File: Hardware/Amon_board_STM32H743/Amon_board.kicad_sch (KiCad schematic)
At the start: 4 parts

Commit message: Update: finished routing of PCB_v3
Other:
- sheet Devices ports: added CLK_S, CS_OF, MISO_S, MOSI_S, MOT, RST, SCL_S, SDA_S; removed CLK, MISO, MOSI, SCL, SDA
- sheet Microcontroller ports: added AN_BAT_EDF, AN_BAT_MAIN, AN_BUCK_5V, AUX_port, BRD_Led, BUCK_EN_5V, BUCK_EN_7V2, CE1, CE2, CLK_S, CSN1, CSN2, CS_EXT, CS_OF, CS_SD, DRDY, IRQ1, IRQ2, LED_Red, LED_White, MISO_RF, MISO_S, MOSI_RF, MOSI_S, MOT, PWM_EDF, PWM_Servo_X+, PWM_Servo_X-, PWM_Servo_Y+, PWM_Servo_Y-, RGB_Led_B, RGB_Led_G, RGB_Led_R, RST, RX_GPS, SCK_RF, SCL_EXT, SCL_S, SDA_EXT, SDA_S, TX_GPS; removed none
- sheet Outputs ports: added AUX_port, CLK_S, MISO_S, MOSI_S; removed CLK_EXT, MISO_EXT, MOSI_EXT, SCL, SDA
- sheet Power ports: added AN_BAT_MAIN; removed AN_BAT_BRD
- note added: "AMON Board v3"
- moved on the sheet: H1, H2, H3, H4

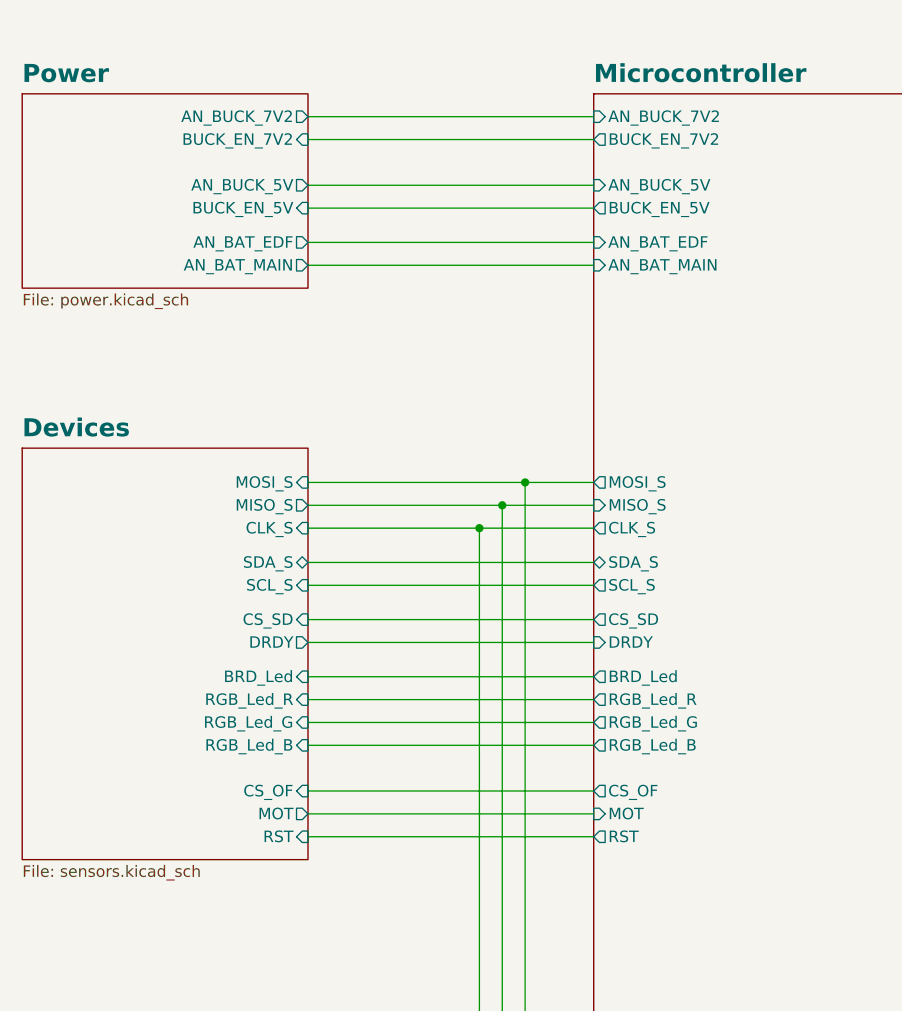
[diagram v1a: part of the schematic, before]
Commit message: Update: finished PCB v3, gerbers, ordered board, readme update
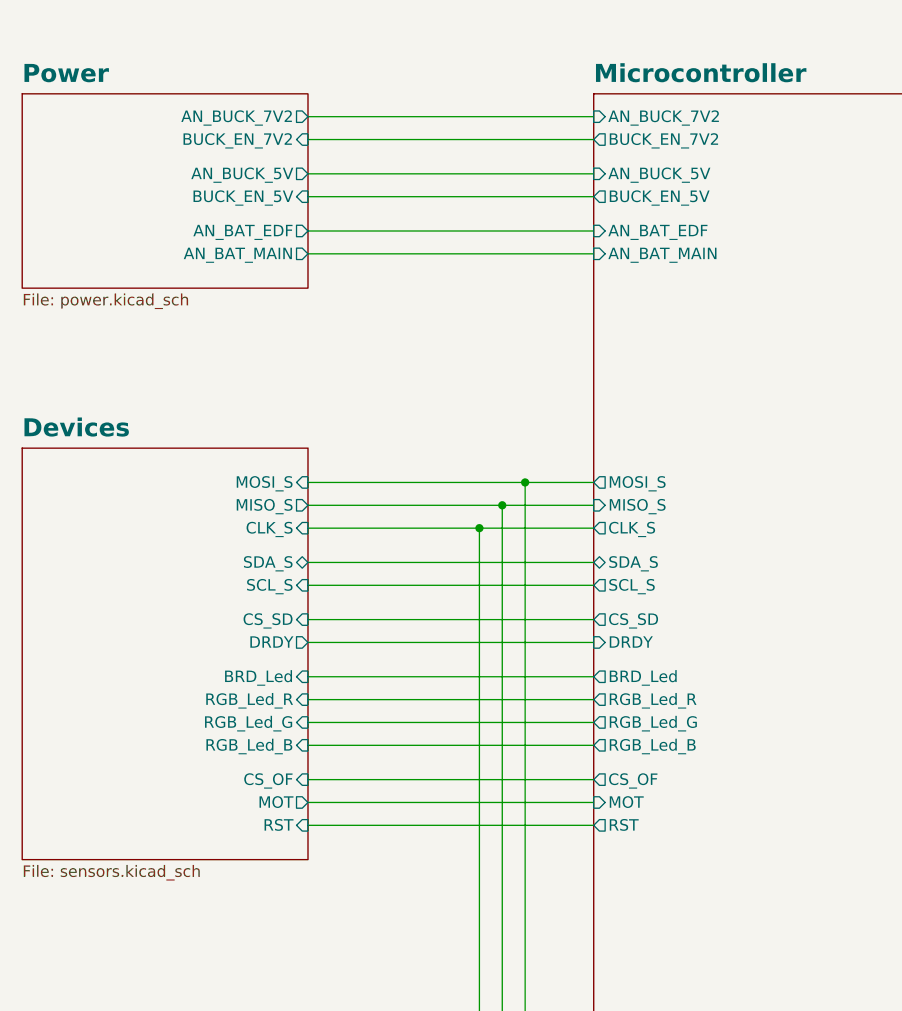
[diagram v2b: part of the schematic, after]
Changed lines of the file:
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@@
 	(wire
 		(pts
-			(xy 74.93 50.8) (xy 106.68 50.8)
+			(xy 74.93 49.53) (xy 106.68 49.53)
 		)
 		(stroke
@@
 	(wire
 		(pts
-			(xy 74.93 118.11) (xy 106.68 118.11)
+			(xy 74.93 116.84) (xy 106.68 116.84)
 		)
 		(stroke
@@
 	(wire
 		(pts
-			(xy 74.93 120.65) (xy 106.68 120.65)
+			(xy 74.93 119.38) (xy 106.68 119.38)
 		)
 		(stroke
@@
 	(wire
 		(pts
-			(xy 74.93 123.19) (xy 106.68 123.19)
+			(xy 74.93 121.92) (xy 106.68 121.92)
 		)
 		(stroke
@@
 	(wire
 		(pts
-			(xy 74.93 57.15) (xy 106.68 57.15)
+			(xy 74.93 55.88) (xy 106.68 55.88)
 		)
 		(stroke
@@
 	(wire
 		(pts
-			(xy 74.93 53.34) (xy 106.68 53.34)
+			(xy 74.93 52.07) (xy 106.68 52.07)
 		)
 		(stroke
@@
 	(wire
 		(pts
-			(xy 74.93 59.69) (xy 106.68 59.69)
+			(xy 74.93 58.42) (xy 106.68 58.42)
 		)
 		(stroke
@@
 		)
 		(pin "BUCK_EN_5V" input
-			(at 74.93 53.34 0)
+			(at 74.93 52.07 0)
 			(effects
 				(font
@@
 		)
 		(pin "AN_BUCK_5V" output
-			(at 74.93 50.8 0)
+			(at 74.93 49.53 0)
 			(effects
 				(font
@@
 		)
 		(pin "AN_BAT_EDF" output
-			(at 74.93 57.15 0)
+			(at 74.93 55.88 0)
 			(effects
 				(font
@@
 		)
 		(pin "AN_BAT_MAIN" output
-			(at 74.93 59.69 0)
+			(at 74.93 58.42 0)
 			(effects
 				(font
@@
 		)
 		(pin "MOT" output
-			(at 74.93 120.65 0)
+			(at 74.93 119.38 0)
 			(effects
 				(font
@@
 		)
 		(pin "RST" input
-			(at 74.93 123.19 0)
+			(at 74.93 121.92 0)
 			(effects
 				(font
@@
 		)
 		(pin "CS_OF" input
-			(at 74.93 118.11 0)
+			(at 74.93 116.84 0)
 			(effects
 				(font
@@
 		)
 		(pin "AN_BUCK_5V" input
-			(at 106.68 50.8 180)
+			(at 106.68 49.53 180)
 			(effects
 				(font
@@
 		)
 		(pin "BUCK_EN_5V" output
-			(at 106.68 53.34 180)
+			(at 106.68 52.07 180)
 			(effects
 				(font
@@
 		)
 		(pin "AN_BAT_EDF" input
-			(at 106.68 57.15 180)
+			(at 106.68 55.88 180)
 			(effects
 				(font
@@
 		)
 		(pin "RST" output
-			(at 106.68 123.19 180)
+			(at 106.68 121.92 180)
 			(effects
 				(font
@@
 		)
 		(pin "MOT" input
-			(at 106.68 120.65 180)
+			(at 106.68 119.38 180)
 			(effects
 				(font
@@
 		)
 		(pin "AN_BAT_MAIN" input
-			(at 106.68 59.69 180)
+			(at 106.68 58.42 180)
 			(effects
 				(font
@@
 		)
 		(pin "CS_OF" output
-			(at 106.68 118.11 180)
-			(effects
-				(font
+			(at 106.68 116.84 180)
+			(effects
+				(font
